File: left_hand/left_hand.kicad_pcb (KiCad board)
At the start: 2 copper layers, 160 x 110 mm, 36 parts, among them K0 SW_Push

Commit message: Put connector on front
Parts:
- moved Left_Plug1 29.4 mm to (187.0, 58.0), turned to 180 degrees
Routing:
- net /Columns4: track 63.1 -> 98.6 mm
- net /Columns3: track 95.9 -> 128.3 mm
- net /Columns0: track 183.2 -> 211.9 mm
- net /Columns1: track 174.5 -> 198.7 mm
- net /Rows1: track 152.3 -> 174.3 mm
- net /Rows2: track 331.6 -> 323.7 mm
- net /Columns2: track 90.3 -> 98.1 mm
- net /Rows0: track 138.7 -> 145.1 mm

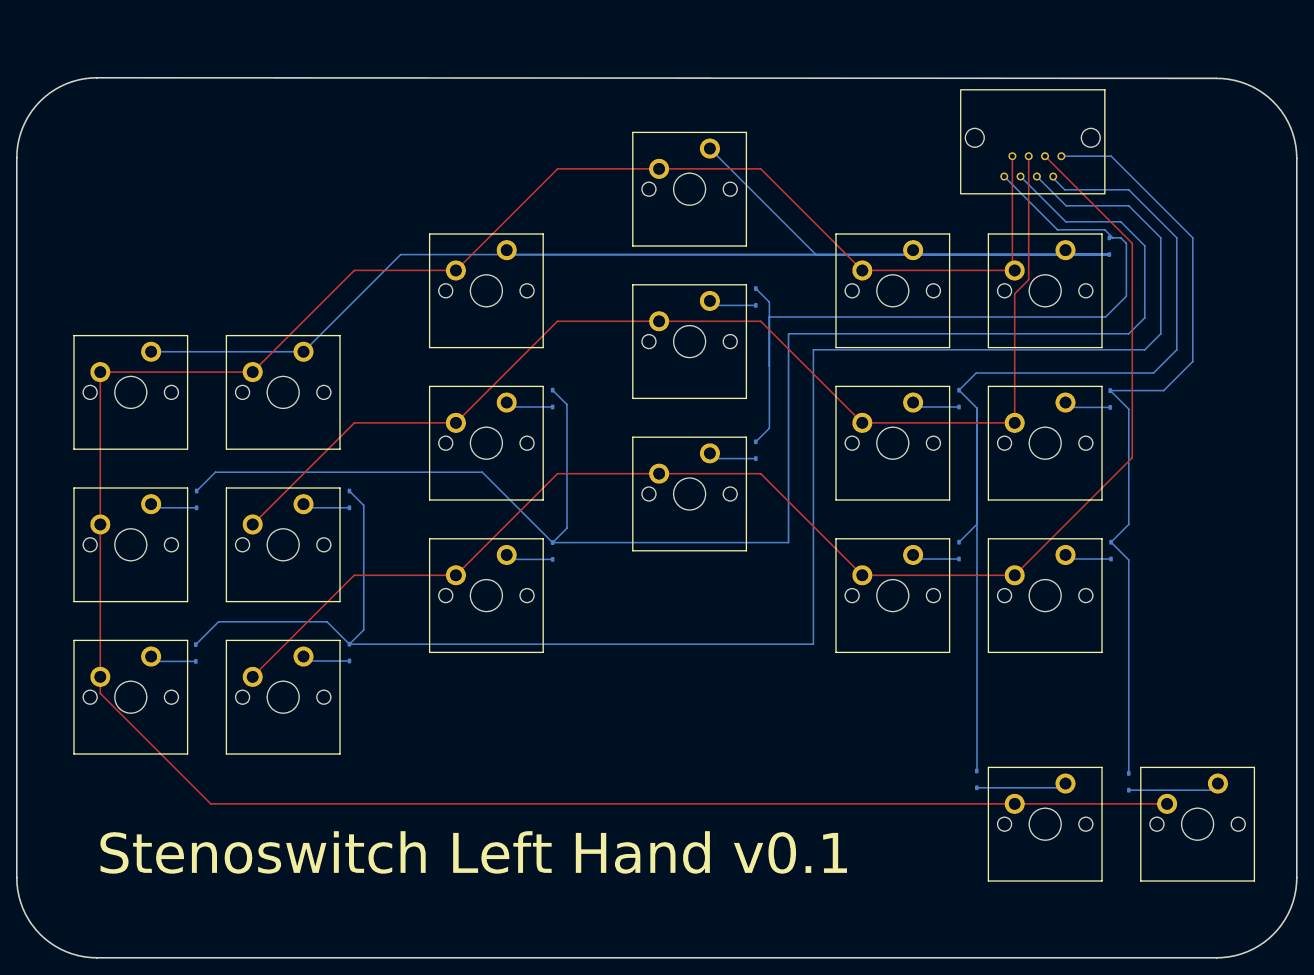
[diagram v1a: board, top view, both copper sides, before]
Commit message: Rework left hand
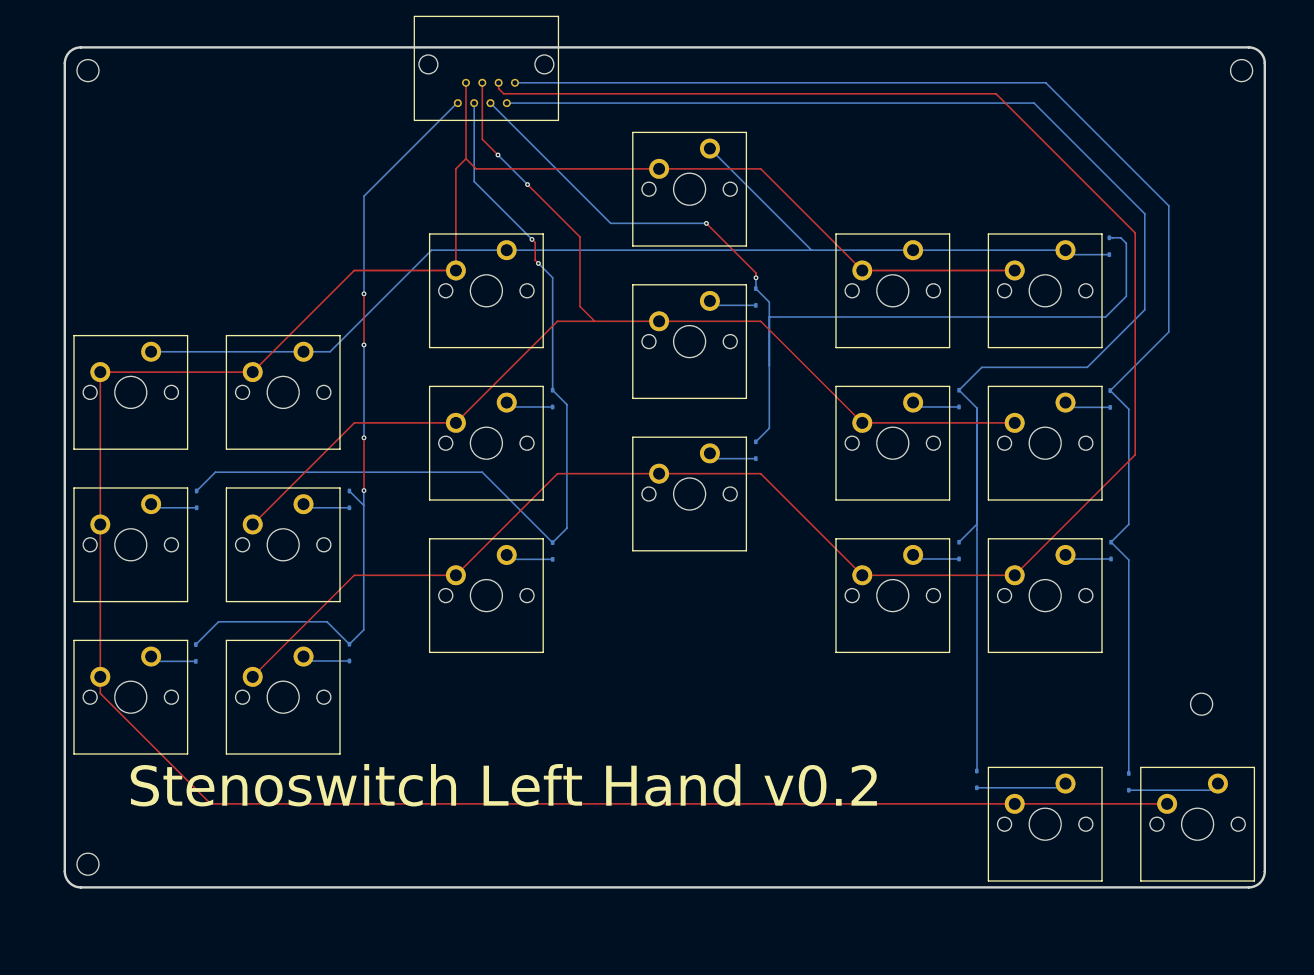
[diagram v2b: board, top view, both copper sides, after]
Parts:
- added ?: , , F.Cu at (68.9, 148.3)
- added ?: , , F.Cu at (208.1, 128.3)
- added ?: , , F.Cu at (68.9, 49.1)
- added ?: , , F.Cu at (213.1, 49.1)
- moved Left_Plug0 68.9 mm to (118.7, 48.8)
- renumbered Left_Plug1 to Left_Plug0
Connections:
- Left_Plug0 pad 2: /Columns0 -> /Columns2
- Left_Plug0 pad 4: /Columns2 -> /Columns0
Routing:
- net Net-(D_{NUM}0-A): track 286.3 -> 144.8 mm
- net /Columns0: track 211.9 -> 97.4 mm, vias 0 -> 4
- net /Columns1: track 198.7 -> 109.6 mm, vias 0 -> 2
- net /Rows1: track 174.3 -> 248.1 mm
- net /Columns4: track 98.6 -> 164.9 mm
- net /Columns3: track 128.3 -> 191.1 mm
- net /Columns2: track 98.1 -> 125.3 mm, vias 0 -> 2
- net /Rows2: track 323.7 -> 327.7 mm
- net /Rows0: track 145.1 -> 146.6 mm, vias 0 -> 2
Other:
- board size 160 x 110 mm -> 150 x 105 mm
- board text added: "*"
- board text added: "Stenoswitch Left Hand v0.2"
- board text removed: "Stenoswitch Left Hand v0.1"

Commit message: Update layout
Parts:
- added ?: , , F.Cu at (99.9, 70.2)
- added ?: , , F.Cu at (144.2, 120.0)
- added ?: , , F.Cu at (169.8, 60.1)
- moved ? 4.58 mm to (212.7, 128.3)
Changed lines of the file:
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@@
 		)
+	)
+	(footprint ""
+		(layer "F.Cu")
+		(at 99.89 70.16)
+		(property "Reference" ""
+			(at 0 0 0)
+			(layer "F.SilkS")
+			(effects
+				(font
+					(size 1.27 1.27)
+					(thickness 0.15)
+				)
+			)
+		)
+		(property "Value" ""
+			(at 0 0 0)
+			(layer "F.Fab")
+			(effects
+				(font
+					(size 1.27 1.27)
+					(thickness 0.15)
+				)
+			)
+		)
+		(property "Datasheet" ""
+			(at 0 0 0)
+			(layer "F.Fab")
+			(hide yes)
+			(effects
+				(font
+					(size 1.27 1.27)
+					(thickness 0.15)
+				)
+			)
+		)
+		(property "Description" ""
+			(at 0 0 0)
+			(layer "F.Fab")
+			(hide yes)
+			(effects
+				(font
+					(size 1.27 1.27)
+					(thickness 0.15)
+				)
+			)
+		)
+		(pad "" np_thru_hole circle
+			(at 0 0 180)
+			(size 2.75 2.75)
+			(drill 2.75)
+			(layers "*.Cu" "*.Mask")
+		)
+		(embedded_fonts no)
 	)
 	(footprint "PCM_Switch_Keyboard_Cherry_MX:SW_Cherry_MX_PCB"
@@
 		)
 	)
+	(footprint ""
+		(layer "F.Cu")
+		(at 144.16 119.98)
+		(property "Reference" ""
+			(at 0 0 0)
+			(layer "F.SilkS")
+			(effects
+				(font
+					(size 1.27 1.27)
+					(thickness 0.15)
+				)
+			)
+		)
+		(property "Value" ""
+			(at 0 0 0)
+			(layer "F.Fab")
+			(effects
+				(font
+					(size 1.27 1.27)
+					(thickness 0.15)
+				)
+			)
+		)
+		(property "Datasheet" ""
+			(at 0 0 0)
+			(layer "F.Fab")
+			(hide yes)
+			(effects
+				(font
+					(size 1.27 1.27)
+					(thickness 0.15)
+				)
+			)
+		)
+		(property "Description" ""
+			(at 0 0 0)
+			(layer "F.Fab")
+			(hide yes)
+			(effects
+				(font
+					(size 1.27 1.27)
+					(thickness 0.15)
+				)
+			)
+		)
+		(pad "" np_thru_hole circle
+			(at 0 0 180)
+			(size 2.75 2.75)
+			(drill 2.75)
+			(layers "*.Cu" "*.Mask")
+		)
+		(embedded_fonts no)
+	)
 	(footprint "PCM_Switch_Keyboard_Cherry_MX:SW_Cherry_MX_PCB"
 		(layer "F.Cu")
@@
 	(footprint ""
 		(layer "F.Cu")
-		(at 208.1 128.3)
+		(at 212.68 128.27)
 		(property "Reference" ""
 			(at 0 0 0)
@@
 		)
 	)
+	(footprint ""
+		(layer "F.Cu")
+		(at 169.77 60.12)
+		(property "Reference" ""
+			(at 0 0 0)
+			(layer "F.SilkS")
+			(effects
+				(font
+					(size 1.27 1.27)
+					(thickness 0.15)
+				)
+			)
+		)
+		(property "Value" ""
+			(at 0 0 0)
+			(layer "F.Fab")
+			(effects
+				(font
+					(size 1.27 1.27)
+					(thickness 0.15)
+				)
+			)
+		)
+		(property "Datasheet" ""
+			(at 0 0 0)
+			(layer "F.Fab")
+			(hide yes)
+			(effects
+				(font
+					(size 1.27 1.27)
+					(thickness 0.15)
+				)
+			)
+		)
+		(property "Description" ""
+			(at 0 0 0)
+			(layer "F.Fab")
+			(hide yes)
+			(effects
+				(font
+					(size 1.27 1.27)
+					(thickness 0.15)
+				)
+			)
+		)
+		(pad "" np_thru_hole circle
+			(at 0 0 180)
+			(size 2.75 2.75)
+			(drill 2.75)
+			(layers "*.Cu" "*.Mask")
+		)
+		(embedded_fonts no)
+	)
 	(footprint "PCM_Switch_Keyboard_Cherry_MX:SW_Cherry_MX_PCB"

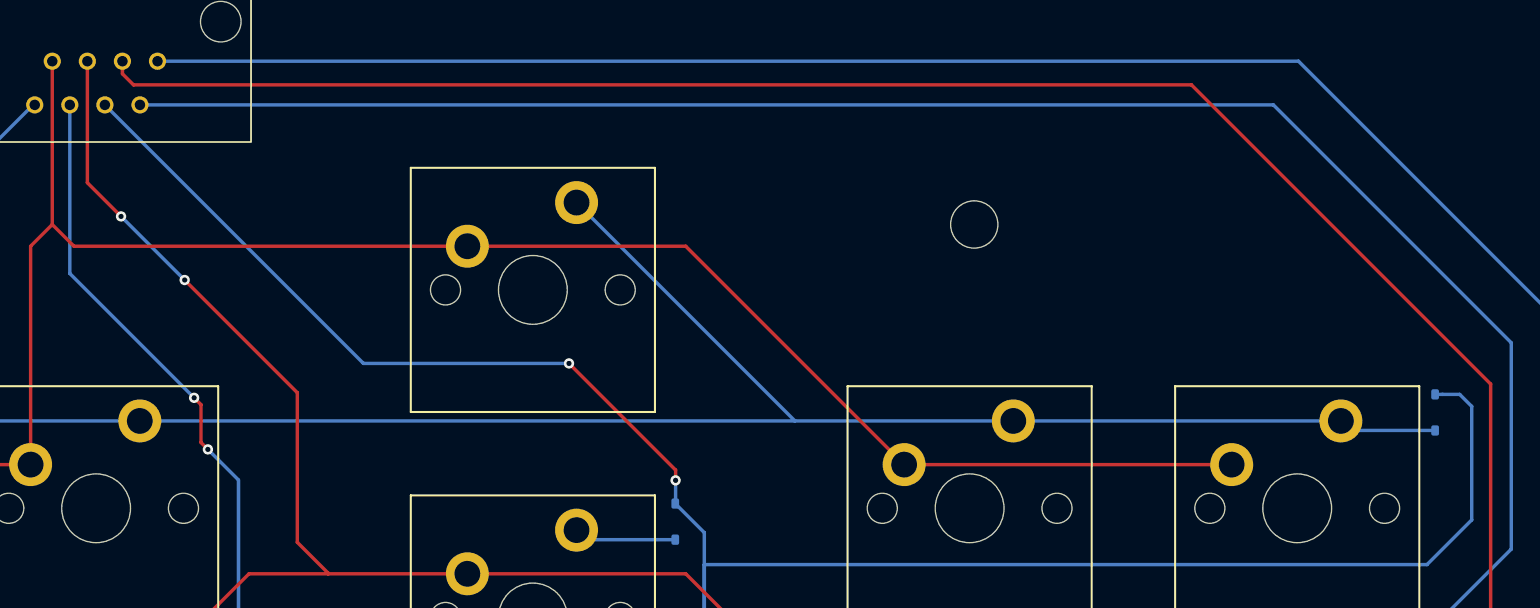
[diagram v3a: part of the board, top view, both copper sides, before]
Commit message: Add holes to stencil
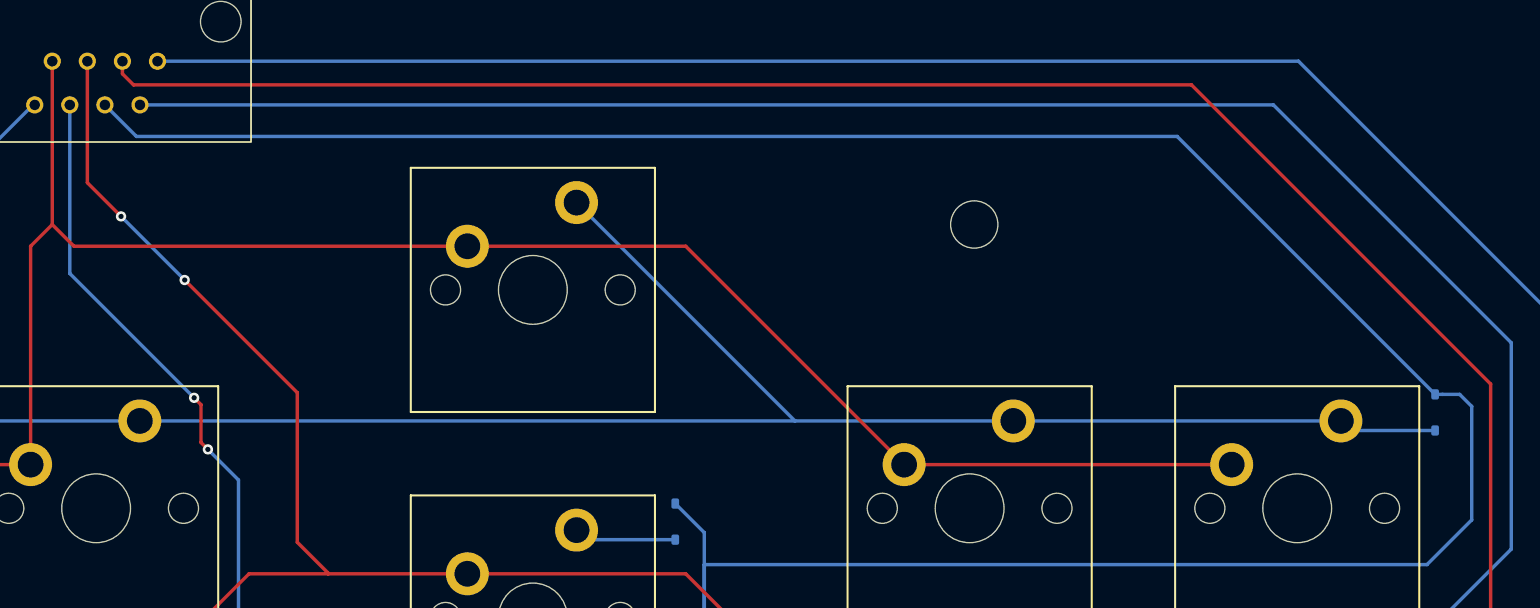
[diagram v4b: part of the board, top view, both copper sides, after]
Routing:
- net /Columns2: track 125.3 -> 165.7 mm, vias 2 -> 0
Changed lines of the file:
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@@
 	(title_block
 		(title "Stenoswitch Left Hand")
-		(date "2025-08-29")
+		(date "2025-09-05")
 		(rev "0.2")
 		(company "https://github.com/Bennett-Petzold/stenoswitch")
@@
 			(drillshape 0)
 			(scaleselection 1)
-			(outputdirectory "../gerbers/")
+			(outputdirectory "../left_hand_gerbers/")
 		)
 	)
@@
 			(size 2.75 2.75)
 			(drill 2.75)
-			(layers "*.Cu" "*.Mask")
+			(layers "*.Cu" "*.Mask" "B.Paste")
 		)
 		(embedded_fonts no)
@@
 			(size 2.75 2.75)
 			(drill 2.75)
-			(layers "*.Cu" "*.Mask")
+			(layers "*.Cu" "*.Mask" "B.Paste")
 		)
 		(embedded_fonts no)
@@
 			(size 2.75 2.75)
 			(drill 2.75)
-			(layers "*.Cu" "*.Mask")
+			(layers "*.Cu" "*.Mask" "B.Paste")
 		)
 		(embedded_fonts no)
@@
 			(size 2.75 2.75)
 			(drill 2.75)
-			(layers "*.Cu" "*.Mask")
+			(layers "*.Cu" "*.Mask" "B.Paste")
 		)
 		(embedded_fonts no)
@@
 	)
 	(segment
-		(start 146.2 68.2)
-		(end 152.4 74.4)
-		(width 0.2)
-		(layer "F.Cu")
-		(net 16)
-	)
-	(segment
-		(start 152.4 74.4)
-		(end 152.4 75)
-		(width 0.2)
-		(layer "F.Cu")
-		(net 16)
-	)
-	(via
-		(at 146.2 68.2)
-		(size 0.6)
-		(drill 0.3)
-		(layers "F.Cu" "B.Cu")
-		(net 16)
-	)
-	(via
-		(at 152.4 75)
-		(size 0.6)
-		(drill 0.3)
-		(layers "F.Cu" "B.Cu")
-		(net 16)
-	)
-	(segment
 		(start 154.07 79.9)
 		(end 196.1 79.9)
@@
 	)
 	(segment
-		(start 119.21 53.165)
-		(end 134.245 68.2)
-		(width 0.2)
-		(layer "B.Cu")
-		(net 16)
-	)
-	(segment
 		(start 198.698955 77.301045)
 		(end 198.698955 70.698955)
@@
 	)
 	(segment
+		(start 196.57 70)
+		(end 181.57 55)
+		(width 0.2)
+		(layer "B.Cu")
+		(net 16)
+	)
+	(segment
 		(start 152.38 95.5)
 		(end 154.07 93.81)
@@
 	)
 	(segment
-		(start 134.245 68.2)
-		(end 146.2 68.2)
-		(width 0.2)
-		(layer "B.Cu")
-		(net 16)
-	)
-	(segment
 		(start 154.07 86)
 		(end 154.07 79.9)
@@
 	)
 	(segment
-		(start 152.4 75)
-		(end 152.4 76.33)
+		(start 198 70)
+		(end 197 70)
 		(width 0.2)
 		(layer "B.Cu")
@@
 	)
 	(segment
-		(start 198 70)
-		(end 197 70)
+		(start 121.045 55)
+		(end 119.21 53.165)
 		(width 0.2)
 		(layer "B.Cu")
@@
 		(width 0.2)
 		(layer "B.Cu")
+		(net 16)
+	)
+	(segment
+		(start 181.57 55)
+		(end 121.045 55)
+		(width 0.2)
+		(layer "B.Cu")
